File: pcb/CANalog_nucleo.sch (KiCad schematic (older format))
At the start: 72 parts, among them J1 USB_B_Micro, J2 PWR, J3 ESP_PROG, J5 AOUT, J6 DSUB9_Male, Q1 DMP3099L-7, Q2 MMBT2222A, SW1 SW_Push, SW2 SW_Push, U1 NUCLEO64-F302R8, U2 BL9342, U3 MCP6002-xSN, U4 SN65HVD230, U5 ESP-12E, U6 OPA330xxDBV, U7 74AHC1G66

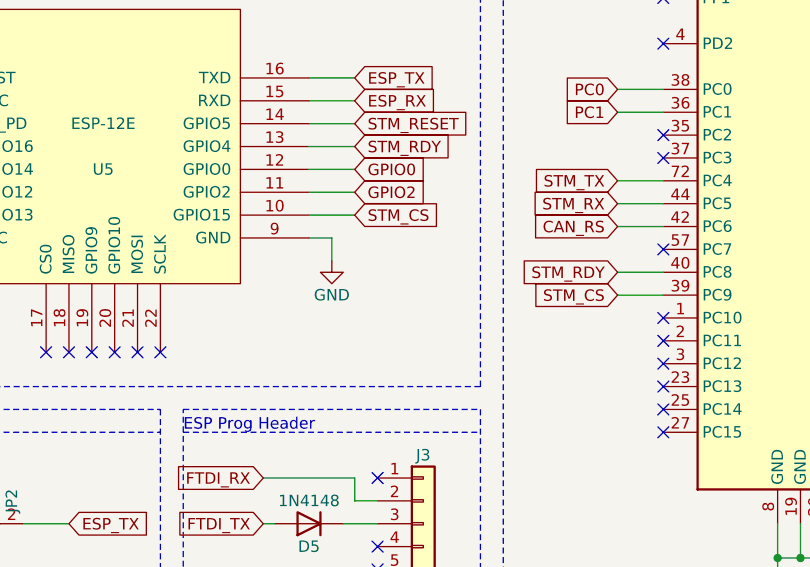
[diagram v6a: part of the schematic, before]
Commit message: add 10k pulldown on GPIO15 of esp
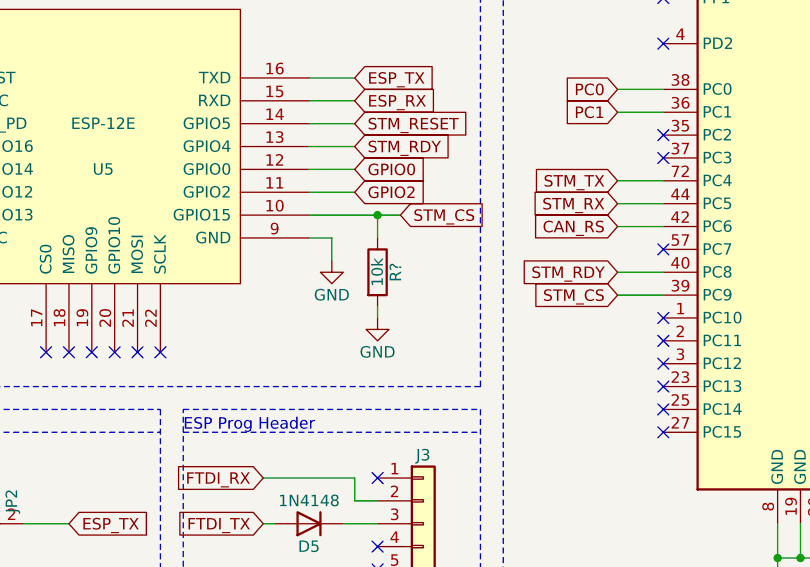
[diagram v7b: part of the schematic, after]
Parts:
- added R?: 10k, symbol Device:R
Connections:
- net GND: now also R?.2
- net STM_CS: now also R?.1
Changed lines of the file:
@@
 $EndComp
 Wire Wire Line
-	5450 5600 5250 5600
-Text GLabel 5450 5600 2    50   Input ~ 0
+	5650 5600 5550 5600
+Text GLabel 5650 5600 2    50   Input ~ 0
 STM_CS
 NoConn ~ 4600 6200
@@
 Wire Wire Line
 	900  3300 900  3250
+$Comp
+L Device:R R?
+U 1 1 604C58E8
+P 5550 5850
+F 0 "R?" V 5630 5850 50  0000 C CNN
+F 1 "10k" V 5550 5850 50  0000 C CNN
+F 2 "" V 5480 5850 50  0001 C CNN
+F 3 "~" H 5550 5850 50  0001 C CNN
+	1    5550 5850
+	1    0    0    -1
+$EndComp
+Wire Wire Line
+	5550 5700 5550 5600
+Connection ~ 5550 5600
+Wire Wire Line
+	5550 5600 5250 5600
+$Comp
+L power:GND #PWR?
+U 1 1 604DFCD5
+P 5550 6050
+F 0 "#PWR?" H 5550 5800 50  0001 C CNN
+F 1 "GND" H 5550 5900 50  0000 C CNN
+F 2 "" H 5550 6050 50  0001 C CNN
+F 3 "" H 5550 6050 50  0001 C CNN
+	1    5550 6050
+	1    0    0    -1
+$EndComp
+Wire Wire Line
+	5550 6050 5550 6000
 $EndSCHEMATC
